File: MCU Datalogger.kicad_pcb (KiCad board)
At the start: 2 copper layers, 48.6 x 32 mm, 30 parts, among them J1 Conn_01x04_Pin, J2 Conn_01x09_Pin, J3 Conn_01x04_Pin, J4 Conn_02x03_Odd_Even, U1 24LC1025, U2 24LC1025, U3 DS1337S_, U4 ATMEGA328P-AU, Y1 32.768 KHz, Y2 16 MHz

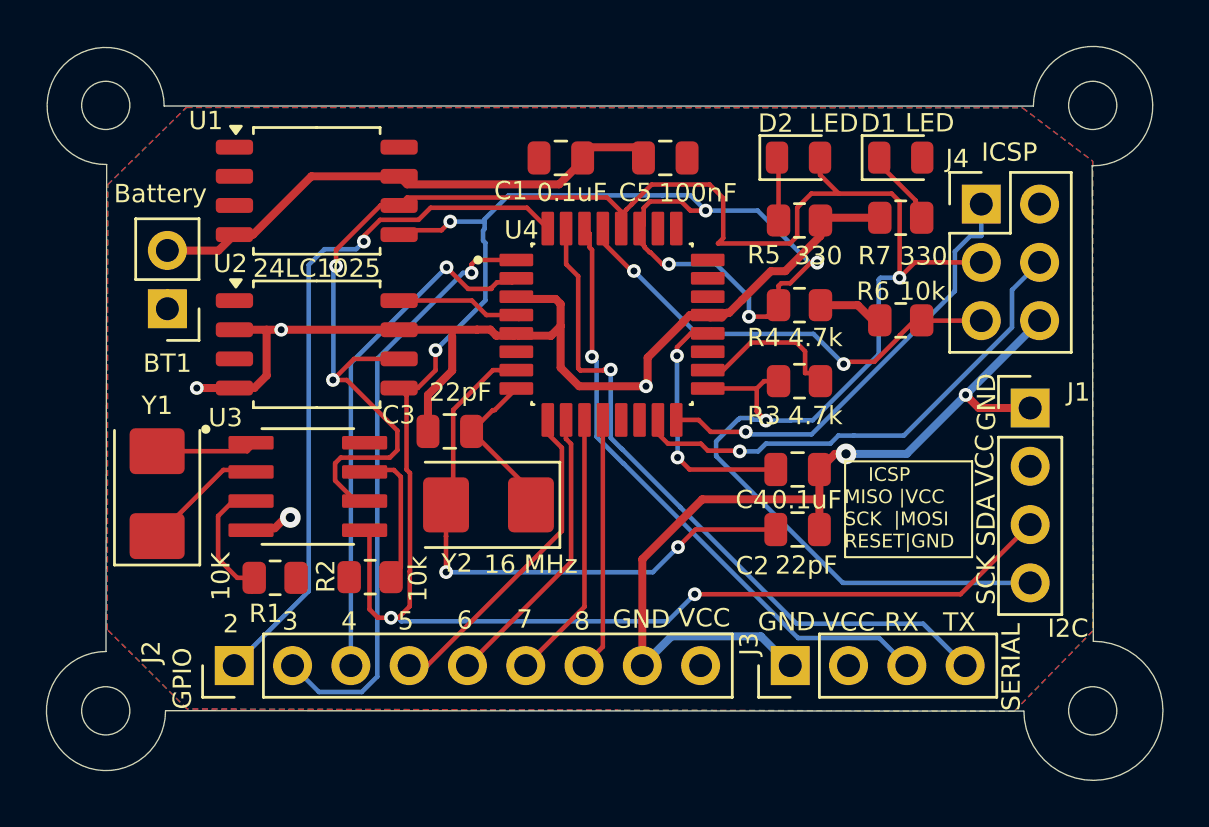
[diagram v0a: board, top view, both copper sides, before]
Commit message: fixing pcb routing after fix the schematic.
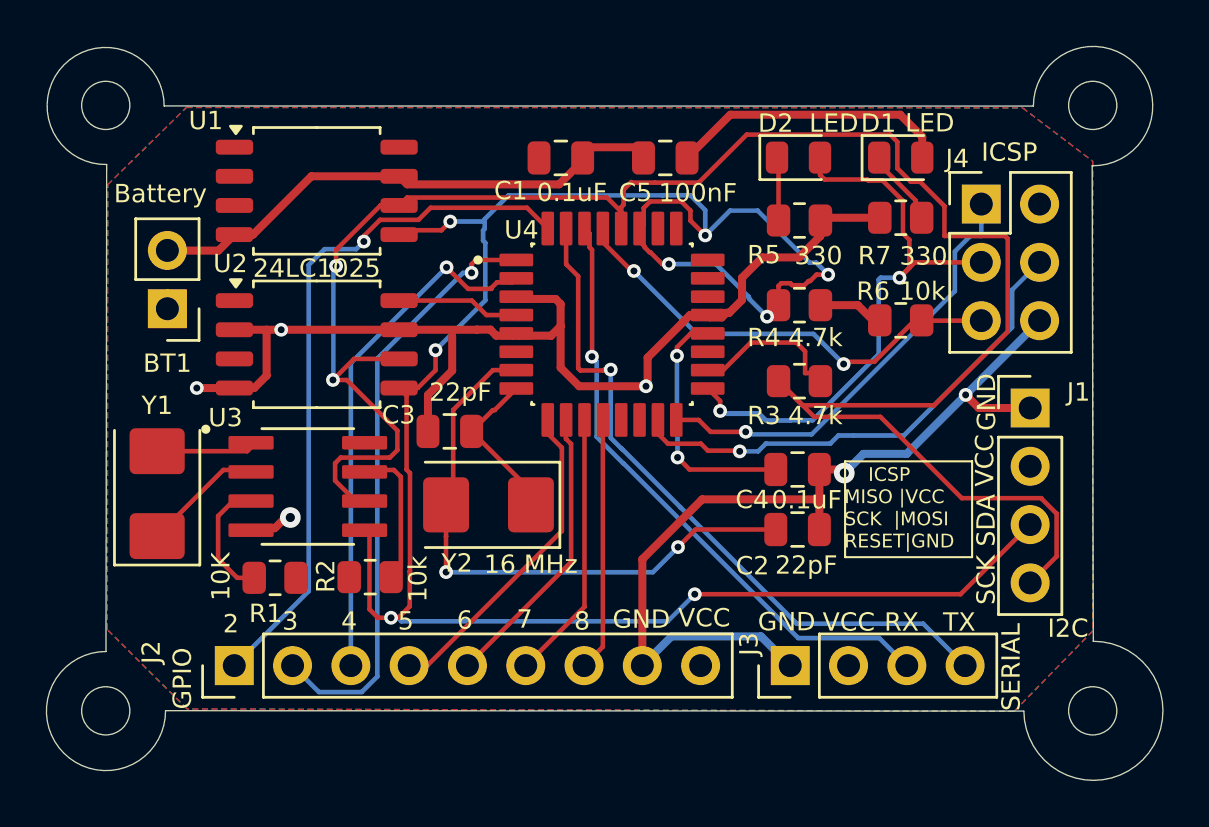
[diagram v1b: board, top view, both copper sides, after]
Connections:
- J1 pad 4: /SCK -> /SCL
- R3 pad 2: /SCK -> /SCL
- U1 pad 6: /SCK -> /SCL
- U2 pad 6: /SCK -> /SCL
- U3 pad 6: /SCK -> /SCL
- U4 pad 28: /SCK -> /SCL
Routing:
- net /SCL: track 0.00 -> 90.5 mm, vias 0 -> 2
- net /SCK: track 95.7 -> 28.4 mm, vias 4 -> 2
- net /Vcc: track 17.5 -> 29.8 mm
- net /SDA: track 90.8 -> 93.6 mm
- net GND: track 112.4 -> 113.1 mm

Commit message: added board characteristics for 2 layer pcb.
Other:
- board text added: "0.2000 mm / 0.0000 mm"
- board text added: "0.3000 mm"
- board text added: "1.6000 mm"
- board text added: "48.6540 mm x 31.9848 mm"
- board text added: "BOARD CHARACTERISTICS"
- board text added: "Board Thickness:"
- board text added: "Board overall dimensions:"
- board text added: "Castellated pads:"
- board text added: "Copper Finish:"
- board text added: "Copper Layer Count:"
- board text added: "Edge card connectors:"
- board text added: "Impedance Control:"
- board text added: "Min hole diameter:"
- board text added: "Min track/spacing:"
- board text added: "No"
- board text added: "None"
- board text added: "Plated Board Edge:"
